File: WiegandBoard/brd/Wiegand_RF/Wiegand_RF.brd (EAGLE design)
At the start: 62.2 x 58.4 mm, 59 parts, among them IC9 LM1117, Q1 NTR1P02T1G, Q2 NTR1P02T1G

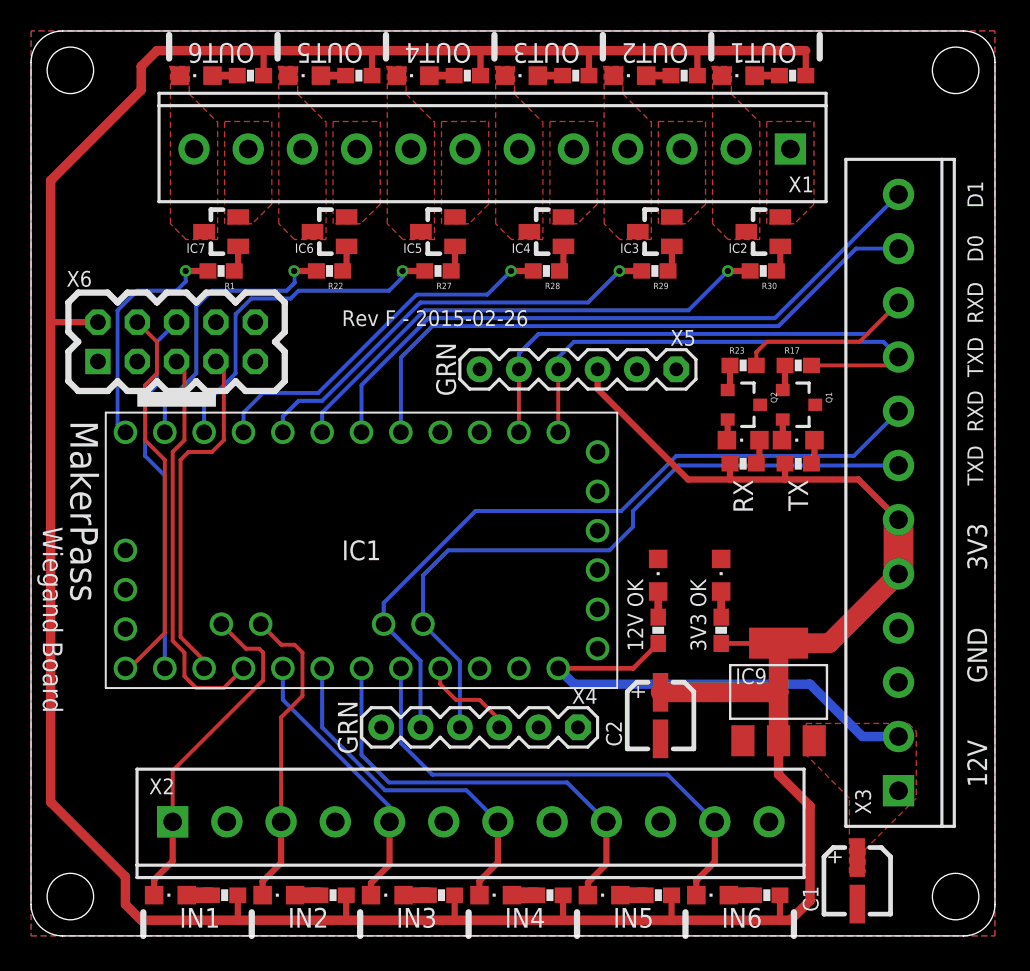
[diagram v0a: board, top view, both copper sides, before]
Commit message: cleaned rs485 files, updated RF version for production - REV F
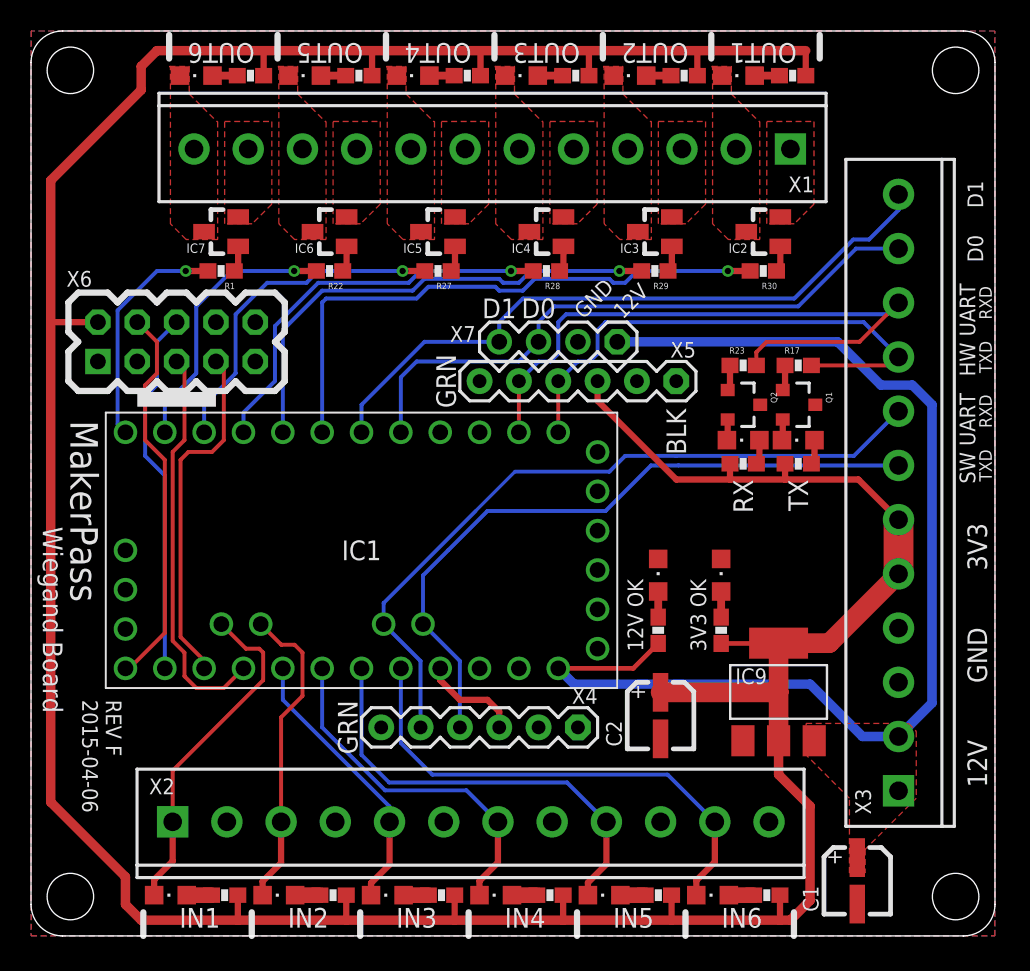
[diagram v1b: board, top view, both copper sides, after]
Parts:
- added X7: (no value), Lumisense:CON-1X4
- moved X5 0.76 mm to (41.7, 35.8)
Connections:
- removed net ARDUINO-D0: IC1.5, X3.11
- removed net ARDUINO-D1: IC1.6, X3.12
- new net ARDUINO-VCC: IC1.21, X4.3
- new net RFID-D0: IC1.5, X3.11, X7.3
- new net RFID-D1: IC1.6, X3.12, X7.4
- net +12V: now also X7.1
- net 3V3: no longer IC1.21, X4.3
- net GND: now also X7.2
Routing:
- net +12V: track 30.9 -> 75.2 mm
- net RFID-D1: track 0.00 -> 43.4 mm
- net ARDUINO-D1: track 42.8 -> 0.00 mm
- net RFID-D0: track 0.00 -> 39.9 mm
- net ARDUINO-D0: track 39.9 -> 0.00 mm
- net 3V3: track 243.8 -> 237.2 mm
- net ARDUINO-VCC: track 0.00 -> 6.43 mm
- net OUTPUT1: track 32.7 -> 37.3 mm
- net OUTPUT2: track 28.1 -> 31.6 mm
- net OUTPUT3: track 23.8 -> 25.8 mm
- net ARDUINO-TXD: track 33.5 -> 34.5 mm
- net ARDUINO-CONSOLE-RX: track 45.0 -> 44.4 mm
- net OUTPUT4: track 22.4 -> 21.8 mm
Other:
- board text added: "BLK"
- board text added: "HW UART"
- board text added: "REV F - 2015-04-06"
- board text added: "REV F 2015-04-06"
- board text added: "SW UART"
- board text removed: "Rev F - 2015-02-26"
